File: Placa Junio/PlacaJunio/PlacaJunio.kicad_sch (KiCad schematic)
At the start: 13 parts, among them IC1 LC86LICMD, J5 Terminal P3, J6 Terminal P4, Q4 IRLML0030, U5 TSR2-2433N

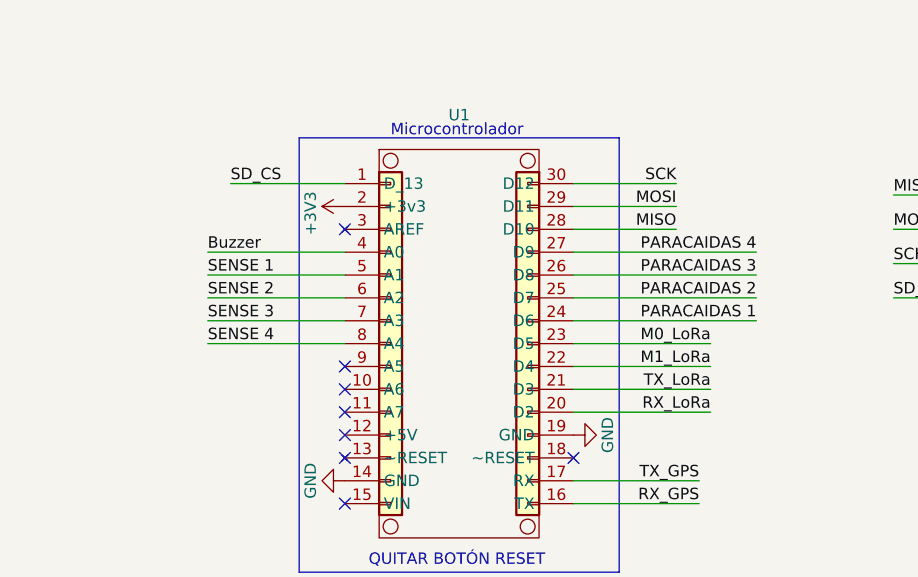
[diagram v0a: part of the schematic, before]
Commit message: Cambio de posición de componenentes
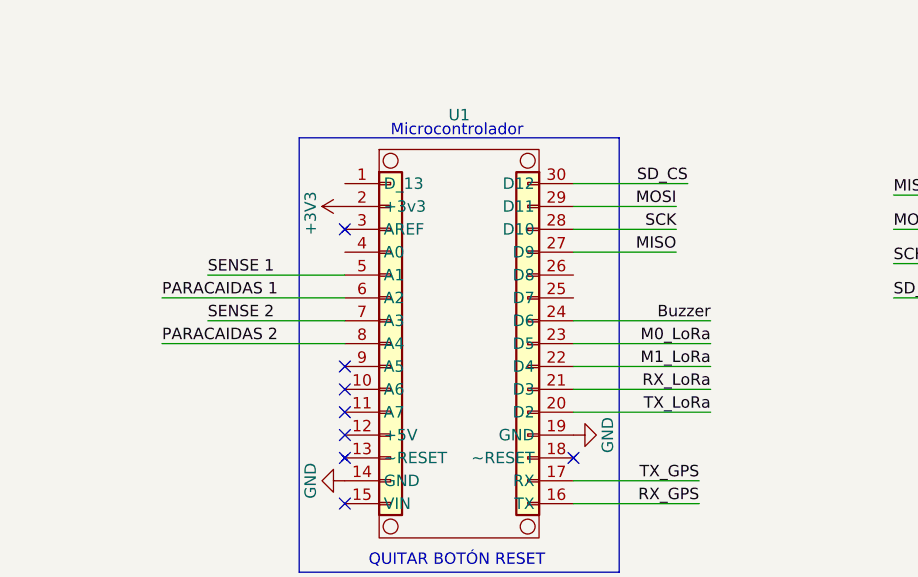
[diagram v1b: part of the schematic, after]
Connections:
- net Buzzer: now also U1.24 (D6); no longer U1.4 (A0)
- net MISO: now also U1.27 (D9); no longer U1.28 (D10)
- net PARACAIDAS 1: now also U1.6 (A2); no longer U1.24 (D6)
- net PARACAIDAS 2: now also U1.8 (A4); no longer U1.25 (D7)
- net PARACAIDAS 3: no longer U1.26 (D8)
- net PARACAIDAS 4: no longer U1.27 (D9)
- net RX_LoRa: now also U1.21 (D3); no longer U1.20 (D2)
- net SCK: now also U1.28 (D10); no longer U1.30 (D12)
- net SD_CS: now also U1.30 (D12); no longer U1.1 (D_13)
- net SENSE 2: now also U1.7 (A3); no longer U1.6 (A2)
- net SENSE 3: no longer U1.7 (A3)
- net SENSE 4: no longer U1.8 (A4)
- net TX_LoRa: now also U1.20 (D2); no longer U1.21 (D3)

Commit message: Ruteando
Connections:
- net +BATT: now also J6.1 (Pin_1); no longer J6.2 (Pin_2)
- net GND: now also J5.2 (Pin_2); no longer J5.1 (Pin_1)
- net M0_LoRa: now also U1.11 (A7); no longer U1.23 (D5)
- net M1_LoRa: now also U1.10 (A6); no longer U1.22 (D4)
- net PARACAIDAS 1: now also U1.5 (A1); no longer U1.6 (A2)
- net PARACAIDAS 2: now also U1.7 (A3); no longer U1.8 (A4)
- net RX_LoRa: now also U1.9 (A5); no longer U1.21 (D3)
- net SENSE 1: now also U1.4 (A0); no longer U1.5 (A1)
- net SENSE 2: now also U1.6 (A2); no longer U1.7 (A3)
- net TX_LoRa: now also U1.8 (A4); no longer U1.20 (D2)
- new net: J5.1 (Pin_1), J6.2 (Pin_2)
- no-connect marks 15 -> 19
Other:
- moved on the sheet: J5, J6

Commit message: Version 1
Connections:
- net Buzzer: now also U1.1 (D_13); no longer U1.24 (D6)
- net PARACAIDAS 1: now also U1.25 (D7); no longer U1.5 (A1)
- net PARACAIDAS 2: now also U1.26 (D8); no longer U1.7 (A3)
- net SENSE 2: now also U1.5 (A1); no longer U1.6 (A2)
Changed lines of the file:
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@@
+	)
+	(no_connect
+		(at 153.67 96.52)
 	)
 	(no_connect
@@
 	)
 	(no_connect
-		(at 153.67 93.98)
-	)
-	(no_connect
 		(at 196.85 129.54)
 	)
 	(no_connect
+		(at 128.27 96.52)
+	)
+	(no_connect
 		(at 128.27 86.36)
 	)
@@
 	)
 	(no_connect
-		(at 128.27 81.28)
+		(at 128.27 93.98)
 	)
 	(no_connect
@@
 	)
 	(no_connect
-		(at 153.67 91.44)
-	)
-	(no_connect
 		(at 196.85 134.62)
 	)
@@
 	(wire
 		(pts
-			(xy 168.91 96.52) (xy 153.67 96.52)
-		)
-		(stroke
-			(width 0)
-			(type default)
-		)
-	)
-	(wire
-		(pts
 			(xy 237.49 137.16) (xy 232.41 137.16)
 		)
@@
 	(wire
 		(pts
-			(xy 113.03 93.98) (xy 128.27 93.98)
+			(xy 113.03 91.44) (xy 128.27 91.44)
+		)
+		(stroke
+			(width 0)
+			(type default)
+		)
+	)
+	(wire
+		(pts
+			(xy 153.67 91.44) (xy 173.99 91.44)
+		)
+		(stroke
+			(width 0)
+			(type default)
+		)
+	)
+	(wire
+		(pts
+			(xy 113.03 81.28) (xy 128.27 81.28)
 		)
 		(stroke
@@
 	(wire
 		(pts
-			(xy 128.27 91.44) (xy 107.95 91.44)
-		)
-		(stroke
-			(width 0)
-			(type default)
-		)
-	)
-	(wire
-		(pts
 			(xy 232.41 142.24) (xy 270.51 142.24)
 		)
@@
 	(wire
 		(pts
+			(xy 153.67 93.98) (xy 173.99 93.98)
+		)
+		(stroke
+			(width 0)
+			(type default)
+		)
+	)
+	(wire
+		(pts
 			(xy 153.67 81.28) (xy 166.37 81.28)
 		)
@@
 		(pts
 			(xy 62.23 40.64) (xy 62.23 41.91)
-		)
-		(stroke
-			(width 0)
-			(type default)
-		)
-	)
-	(wire
-		(pts
-			(xy 128.27 96.52) (xy 107.95 96.52)
 		)
 		(stroke
@@
 		)
 	)
+	(label "PARACAIDAS 1"
+		(at 173.99 93.98 180)
+		(effects
+			(font
+				(size 1.27 1.27)
+			)
+			(justify right bottom)
+		)
+	)
 	(label "Buzzer"
-		(at 168.91 96.52 180)
-		(effects
-			(font
-				(size 1.27 1.27)
-			)
-			(justify right bottom)
+		(at 113.03 81.28 0)
+		(effects
+			(font
+				(size 1.27 1.27)
+			)
+			(justify left bottom)
 		)
 	)
@@
 	)
 	(label "SENSE 2"
-		(at 113.03 93.98 0)
+		(at 113.03 91.44 0)
 		(effects
 			(font
@@
 		)
 	)
+	(label "PARACAIDAS 2"
+		(at 173.99 91.44 180)
+		(effects
+			(font
+				(size 1.27 1.27)
+			)
+			(justify right bottom)
+		)
+	)
 	(label "RX_LoRa"
 		(at 113.03 101.6 0)
@@
 		)
 	)
-	(label "PARACAIDAS 1"
-		(at 107.95 91.44 0)
-		(effects
-			(font
-				(size 1.27 1.27)
-			)
-			(justify left bottom)
-		)
-	)
 	(label "MOSI"
 		(at 189.23 86.36 0)
@@
 		(effects
 			(font
-				(size 1.27 1.27)
-			)
-			(justify left bottom)
-		)
-	)
-	(label "PARACAIDAS 2"
-		(at 107.95 96.52 0)
-		(effects
-			(font

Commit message: Primera versión definitiva
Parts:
- added J1: Conn_01x07_Pin, Connector_PinHeader_2.54mm:PinHeader_1x07_P2.54mm_Vertical, symbol Connector:Conn_01x07_Pin
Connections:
- net +3V3: now also J1.1 (Pin_1)
- net GND: now also J1.7 (Pin_7)
- net D2: now reaches U1.20 (D2)
- net D2: now also J1.6 (Pin_6)
- net D3: now reaches U1.21 (D3)
- net D3: now also J1.5 (Pin_5)
- net D4: now reaches U1.22 (D4)
- net D4: now also J1.4 (Pin_4)
- net D5: now reaches U1.23 (D5)
- net D5: now also J1.3 (Pin_3)
- net D6: now reaches U1.24 (D6)
- net D6: now also J1.2 (Pin_2)
- no-connect marks 19 -> 14
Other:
- note added: "AÑADIR DIODO"
- note added: "Conector externo"
- moved on the sheet: BZ1, C6, C7, IC1, Q4, R9, U3

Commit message: V1 definitiva
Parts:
- added D1: D, Diode_SMD:D_0805_2012Metric, symbol Device:D
- added H1, H2, H3, H4: MountingHole, MountingHole:MountingHole_3.2mm_M3_DIN965, symbol Mechanical:MountingHole
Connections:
- net +3V3: now also D1.1 (K)
- net at BZ1.2 (-), Q4.3 (D): now also D1.2 (A)
- net Aux: now reaches U1.7 (A3)
- net Aux: now also U3.5 (AUX)
- no-connect marks 14 -> 12
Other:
- note added: "Agujeros para tornillos"
- note removed: "AÑADIR DIODO"
- moved on the sheet: BZ1, Q4, R9
